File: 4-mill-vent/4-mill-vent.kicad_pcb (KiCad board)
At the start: 2 copper layers, 87 x 47.6 mm, 69 parts, among them J1 Fan, J2 Buszzer, J3 Power, J4 ICSP, Q1 MMBT3904, Q2 MMBT3904, Q3 PZT3904, Q4 PZT3904, Q5 TSM480P06CP, Q6 MMBT3904, SW1 Power_off, SW2 Power_On, SW3 Fan_Down, SW4 Fan_Up, U1 LM321, U2 TSR_1-24120, U3 LM1117-5.0, U4 ATmega328P-AU, Y1 16.000MHZ

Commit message: Save point
Lots done, still working on some of the design so parts of micro are still up in air. Looks like this board size will for and can be made smaller
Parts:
- added C15: C0603C104M4RACTU, Capacitor_SMD:C_0603_1608Metric, F.Cu at (290.1, 172.7)
- added C16: C0603C104M4RACTU, Capacitor_SMD:C_0603_1608Metric, F.Cu at (283.4, 172.7)
- added R22: 10k, Resistor_SMD:R_0603_1608Metric, F.Cu at (283.4, 174.6)
- added R23: 10k, Resistor_SMD:R_0603_1608Metric, F.Cu at (290.1, 174.6)
- J2: value Buszzer -> Buzzer
- moved R12 102.2 mm to (322.8, 158.2)
- moved Q4 97.7 mm to (322.4, 167.5)
- moved Motor1 96.3 mm to (323.6, 181.0)
- moved D2 96.2 mm to (322.3, 176.5)
- moved R11 96.0 mm to (322.5, 153.4)
- moved R1 81.3 mm to (322.1, 148.9)
- moved R20 80.0 mm to (290.9, 169.1)
- moved C13 78.8 mm to (299.8, 153.7), turned to 270 degrees
- moved R19 75.6 mm to (282.6, 169.1)
- moved R21 64.6 mm to (280.5, 153.9), turned to 90 degrees
- moved J4 62.2 mm to (272.7, 156.2), turned to 180 degrees
- moved C12 47.0 mm to (248.1, 167.9)
- moved C2 47.0 mm to (250.4, 177.8)
- moved C3 47.0 mm to (251.0, 180.5)
- moved C5 47.0 mm to (250.2, 168.6)
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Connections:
- J2 pad 1: SW_Batt -> Buzzer-
- J2 pad 2: Buzzer- -> SW_Batt
- J3 pad 1: Net-(D13-Pad1) -> Net-(D13-Pad2)
- J3 pad 3: Net-(D13-Pad2) -> Net-(D13-Pad1)
- R19 pad 1: Down -> Net-(C16-Pad1)
- R20 pad 1: Up -> Net-(C15-Pad1)
- SW3 pad 2: Down -> Net-(C16-Pad1)
- SW4 pad 2: Up -> Net-(C15-Pad1)
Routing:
- net Monitor: track 23.2 -> 54.2 mm, vias 0 -> 1
- net +5V: track 116.0 -> 141.2 mm, vias 5 -> 6
- net Net-(R12-Pad1): track 24.8 -> 0.00 mm
- net Net-(D2-Pad2): track 19.8 -> 0.00 mm
- net Down: track 12.4 -> 0.00 mm, vias 1 -> 0
- net Buzzer-: track 26.5 -> 16.7 mm
- net Net-(Q5-Pad1): track 6.53 -> 15.6 mm
- net Net-(D2-Pad1): track 8.34 -> 0.00 mm
- net Net-(C15-Pad1): track 0.00 -> 7.66 mm
- net Net-(C16-Pad1): track 0.00 -> 7.50 mm
- net Up: track 6.49 -> 0.00 mm, vias 1 -> 0
- net Net-(Q3-Pad1): track 1.65 -> 7.80 mm
- net Net-(Q4-Pad1): track 5.69 -> 0.00 mm
- net Reset: track 3.28 -> 8.03 mm
- net Raw_Batt: track 35.9 -> 31.9 mm, vias 3 -> 2
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
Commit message: Just pushing updates
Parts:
- moved D8 0.23 mm to (277.7, 153.6)
- moved D9 0.20 mm to (286.8, 153.7)
- moved R21 0.16 mm to (280.5, 153.7)
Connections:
- R23 pad 1: Net-(R23-Pad1) -> Up
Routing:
- net Up: track 0.00 -> 30.8 mm, vias 0 -> 1
- net Down: track 0.00 -> 28.9 mm, vias 0 -> 1
- net +5V: track 141.2 -> 167.4 mm
- net +12V: track 46.5 -> 53.6 mm
- net Net-(C15-Pad1): track 7.66 -> 14.0 mm
- net GND: vias 42 -> 43

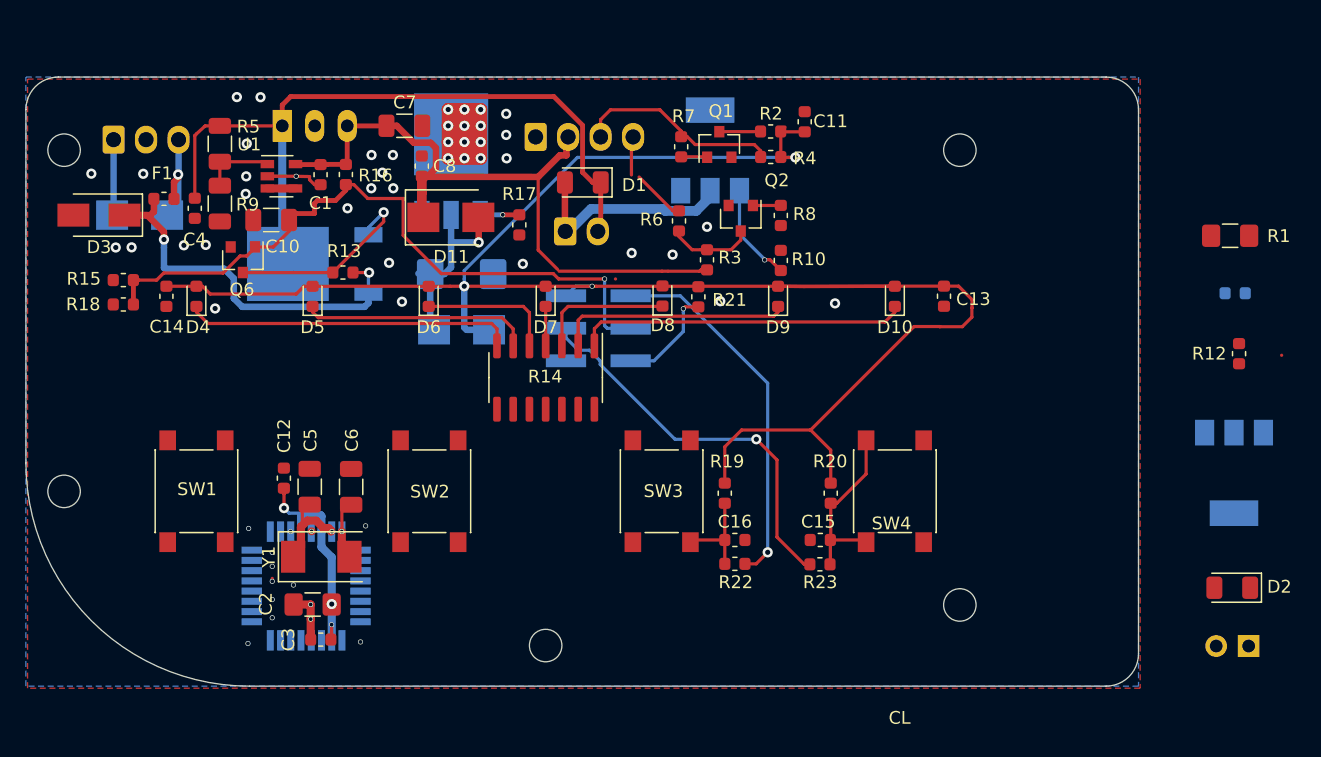
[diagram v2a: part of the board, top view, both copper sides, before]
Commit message: Just an update on things
update schematic to and pcb. figured out a way to user int, ext and chager over three pin connector with only to wires to PCB and no extra diode needed. getting closer to the anwers on PWM pins to use with what fuction.
very little let to do on PCB, but things have to get checked before getting it done.
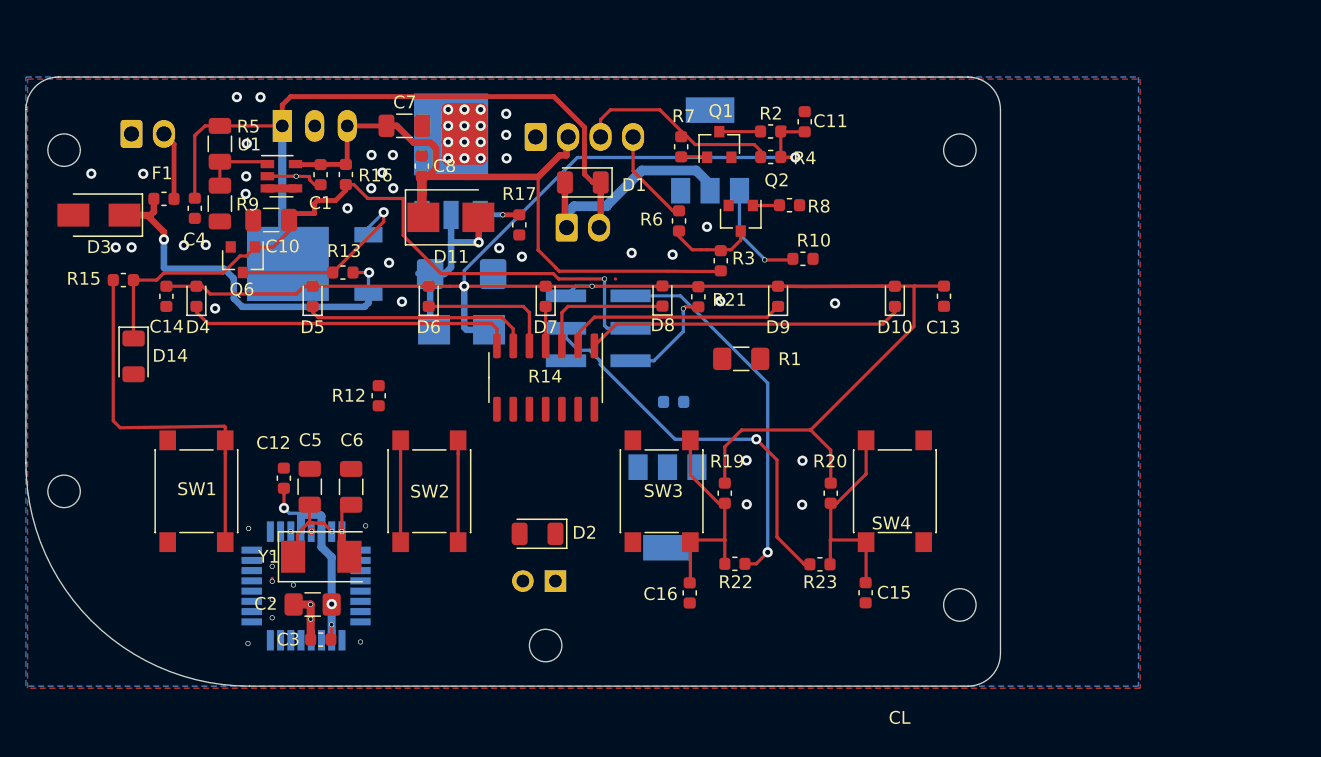
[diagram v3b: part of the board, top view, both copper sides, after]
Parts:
- removed D13: FM4004-W, Diode_SMD:D_SMB
- removed R18: 1k, Resistor_SMD:R_0603_1608Metric
- added D14: 1N914, Diode_SMD:D_1206_3216Metric, F.Cu at (236.4, 158.4)
- D3: value SML4752HE3_A/I -> 833-3SMAJ5936B-TP
- J3: value Power -> POWER_CONNECTOR; footprint Connector_Molex:Molex_KK-254_AE-6410-03A_1x03_P2.54mm_Vertical -> Connector_Molex:Molex_KK-254_AE-6410-02A_1x02_P2.54mm_Vertical
- U2: value TSR_1-24120 -> TPSM84212EAB
- moved R12 67.4 mm to (255.5, 161.4)
- moved D2 54.5 mm to (268.0, 172.2)
- moved Motor1 54.4 mm to (269.4, 175.9)
- moved R11 44.7 mm to (278.6, 161.9), turned to 180 degrees
- moved Q4 44.4 mm to (278.1, 170.2)
- moved R1 39.4 mm to (283.9, 158.6)
- moved C15 5.44 mm to (293.6, 176.8), turned to 270 degrees
- moved C16 5.44 mm to (279.9, 176.9), turned to 270 degrees
- moved R10 1.74 mm to (288.7, 150.7), turned to 0 degrees
- moved J3 1.47 mm to (236.2, 141.0)
- moved R3 1.08 mm to (282.3, 150.9)
- moved R8 1.05 mm to (287.7, 146.5), turned to 180 degrees
- moved J2 0.31 mm to (270.2, 148.3)
- turned U4 to 0 degrees
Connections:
- C10 pad 1: Monitor -> Monitor_SCLK
- F1 pad 1: Net-(D13-Pad1) -> Net-(F1-Pad1)
- J3 pad 1: Net-(D13-Pad2) -> GND
- J3 pad 2: GND -> Net-(F1-Pad1)
- J4 pad 1: Down -> Up_MOSI
- J4 pad 3: Monitor -> Monitor_SCLK
- J4 pad 4: Up -> Down+MOSO
- Q6 pad 1: Monitor -> Monitor_SCLK
- R15 pad 1: Monitor -> Monitor_SCLK
- R16 pad 1: Monitor -> Monitor_SCLK
- R22 pad 2: Down -> Down+MOSO
- R23 pad 1: Up -> Up_MOSI
- SW2 pad 1: Net-(R15-Pad2) -> Monitor_SCLK
- U4 pad 12: Monitor -> Net-(U4-Pad12)
- U4 pad 13: Motor -> Net-(U4-Pad13)
- U4 pad 15: Up -> Up_MOSI
- U4 pad 16: Down -> Down+MOSO
- U4 pad 17: Monitor -> Monitor_SCLK
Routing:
- net Net-(R15-Pad2): track 0.00 -> 29.0 mm
- net Net-(C16-Pad1): track 7.50 -> 17.0 mm
- net Net-(D13-Pad1): track 8.05 -> 0.00 mm, vias 2 -> 1
- net Net-(R12-Pad1): track 0.00 -> 7.96 mm
- net Monitor_SCLK: track 0.00 -> 7.96 mm
- net Net-(D13-Pad2): track 5.95 -> 0.00 mm
- net +5V: track 167.4 -> 161.8 mm
- net Net-(F1-Pad1): track 0.00 -> 5.41 mm
- net Net-(C5-Pad1): track 11.9 -> 7.88 mm
- net Net-(C15-Pad1): track 14.0 -> 17.2 mm
- net Monitor: track 54.2 -> 56.9 mm
- net Buzzer-: track 16.7 -> 18.5 mm
- net Net-(D9-Pad1): track 18.3 -> 17.5 mm
- net Net-(D10-Pad1): track 25.8 -> 25.0 mm
- net +12V: track 53.6 -> 54.3 mm
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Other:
- board size 87 x 47.6 mm -> 76.2 x 47.6 mm

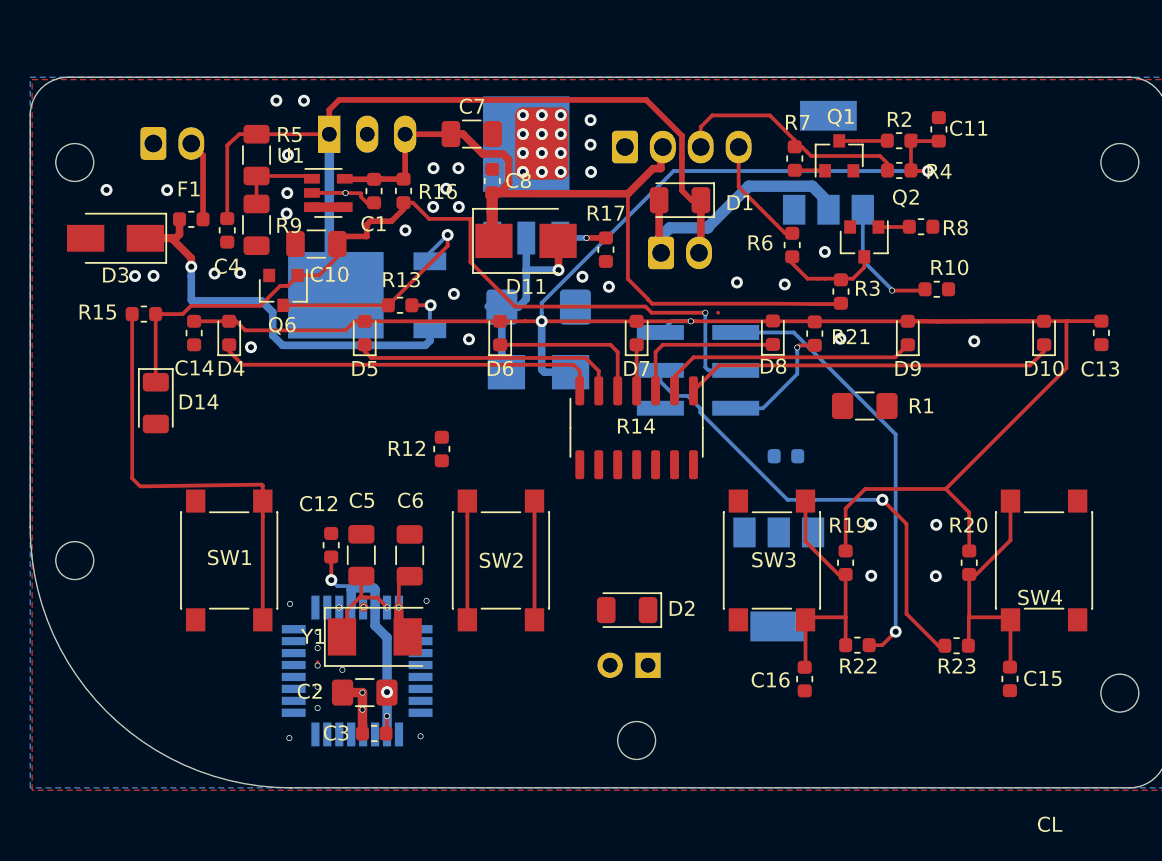
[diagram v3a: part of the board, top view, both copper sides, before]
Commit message: Board mainly done
Layout is done, have things to correct and adjustments to make, but for the most part it is done.
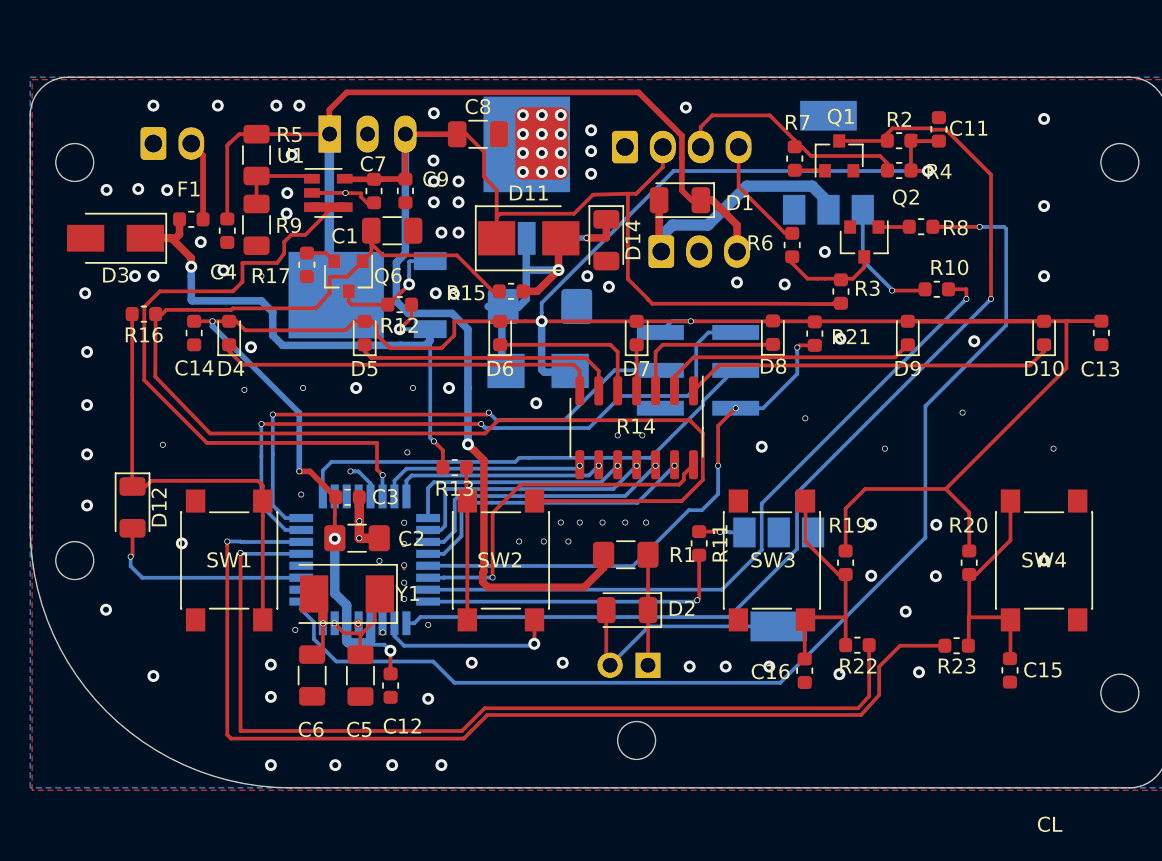
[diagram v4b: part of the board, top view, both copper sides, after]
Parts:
- added D13: FM4004-W, Diode_SMD:D_SMB, B.Cu at (262.0, 156.2)
- C10: value 1uF -> T491C107M006AT; footprint Capacitor_SMD:C_1206_3216Metric -> Capacitor_Tantalum_SMD:CP_EIA-6032-15_Kemet-U; moved to B.Cu
- C7: value LMK316AB7106MLHT -> 3.3uF
- C8: value C0603C104M4RACTU -> LMK316AB7106MLHT; footprint Capacitor_SMD:C_0603_1608Metric -> Capacitor_SMD:C_1206_3216Metric
- C9: value T491C107M006AT -> C0603C104M4RACTU; footprint Capacitor_Tantalum_SMD:CP_EIA-6032-15_Kemet-U -> Capacitor_SMD:C_0603_1608Metric; moved to F.Cu
- D12: value FM4004-W -> 1N914; footprint Diode_SMD:D_SMB -> Diode_SMD:D_1206_3216Metric; moved to F.Cu
- J2: footprint Connector_Molex:Molex_KK-254_AE-6410-02A_1x02_P2.54mm_Vertical -> Connector_Molex:Molex_KK-254_AE-6410-03A_1x03_P2.54mm_Vertical
- J3: value POWER_CONNECTOR -> Power
- R11: moved to F.Cu
- R12: value 100k -> 560k
- R15: value 1M -> 820k
- R16: value 10k -> 220k
- R17: value 47 -> 560k
- R5: value RN73H2BTTD4702B10 -> RN73H2BTTD4322F100
- R9: value RN73H2BTTD7061B10 -> RN73H2BTTD8061F50
- moved D14 32.1 mm to (266.6, 147.4)
- moved D12 28.7 mm to (234.8, 165.4), turned to 270 degrees
- moved R15 24.7 mm to (260.2, 150.9), turned to 0 degrees
- moved R17 20.1 mm to (246.5, 149.1), turned to 270 degrees
- moved R16 19.3 mm to (235.6, 152.4), turned to 180 degrees
- moved R1 18.9 mm to (267.9, 168.5)
- moved C3 15.9 mm to (249.2, 164.7), turned to 180 degrees
- moved C10 15.6 mm to (262.1, 151.9), turned to 0 degrees
- moved C9 11.8 mm to (253.1, 144.1), turned to 270 degrees
- moved R13 11.5 mm to (256.4, 162.7)
- moved C6 10.4 mm to (246.9, 176.6), turned to 270 degrees
- moved C2 10.4 mm to (249.9, 167.4), turned to 180 degrees
- moved C12 10.2 mm to (252.1, 177.3), turned to 270 degrees
- moved R12 10.1 mm to (252.7, 151.8), turned to 180 degrees
- moved C7 8.39 mm to (252.2, 146.8)
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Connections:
- net REF renamed Net-(U4-Pad20)
- C10 pad 1: Monitor_SCLK -> Net-(C10-Pad1)
- C7 pad 1: +12V -> Monitor
- C9 pad 1: Net-(C9-Pad1) -> +12V
- D11 pad 2: Net-(C9-Pad1) -> Net-(C10-Pad1)
- D12 pad 1: +5V -> Net-(D12-Pad1)
- D12 pad 2: Net-(C9-Pad1) -> Micro_power_Down
- D14 pad 1: Monitor -> Net-(D14-Pad1)
- D14 pad 2: Micro_power_Down -> GND
- J2 pad 2: SW_Batt -> Net-(J2-Pad2)
- J4 pad 1: Up_MOSI -> MOSI
- J4 pad 3: Monitor_SCLK -> SCLK
- J4 pad 4: Down+MOSO -> MOSO
- Q6 pad 1: Monitor_SCLK -> Monitor
- Q6 pad 2: GND -> Net-(Q6-Pad2)
- R12 pad 1: Net-(R12-Pad1) -> Raw_Batt
- R12 pad 2: Raw_Batt -> Net-(Q5-Pad1)
- R13 pad 1: Raw_Batt -> Net-(R13-Pad1)
- R13 pad 2: Net-(Q5-Pad1) -> Raw_Batt
- R14 pad 11: Error -> LED4
- R15 pad 1: Monitor_SCLK -> Monitor
- R15 pad 2: Net-(R15-Pad2) -> Net-(C10-Pad1)
- R16 pad 1: Monitor_SCLK -> Monitor
- R16 pad 2: +12V -> Net-(D12-Pad1)
- R17 pad 1: GND -> Net-(Q6-Pad2)
- R17 pad 2: Net-(R17-Pad2) -> GND
- R22 pad 2: Down+MOSO -> Down
- R23 pad 1: Up_MOSI -> Up
- SW1 pad 2: Net-(R15-Pad2) -> Net-(D12-Pad1)
- SW2 pad 1: Monitor_SCLK -> Monitor
- SW2 pad 2: Net-(R12-Pad1) -> Net-(R13-Pad1)
- U3 pad 1: Net-(R17-Pad2) -> Net-(D14-Pad1)
- U3 pad 2: Net-(C9-Pad1) -> Net-(C10-Pad1)
- U4 pad 1: Net-(U4-Pad1) -> RPM
- U4 pad 11: Net-(U4-Pad11) -> Micro_power_Down
- U4 pad 13: Net-(U4-Pad13) -> Down
- U4 pad 14: Net-(U4-Pad14) -> Up
- U4 pad 15: Up_MOSI -> MOSI
- U4 pad 16: Down+MOSO -> MOSO
- U4 pad 17: Monitor_SCLK -> SCLK
- U4 pad 2: Net-(U4-Pad2) -> Monitor
- U4 pad 23: Net-(U4-Pad23) -> LED1
- U4 pad 24: Net-(U4-Pad24) -> LED2
- U4 pad 25: Net-(U4-Pad25) -> LED3
- U4 pad 26: Net-(U4-Pad26) -> LED4
- U4 pad 27: Net-(U4-Pad27) -> LED5
- U4 pad 28: Net-(U4-Pad28) -> LED6
- U4 pad 30: Net-(U4-Pad30) -> LED7
- U4 pad 31: Net-(U4-Pad31) -> Alarm
- U4 pad 32: Net-(U4-Pad32) -> Motor
- U4 pad 9: Net-(U4-Pad9) -> PWM
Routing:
- net PWM: track 0.00 -> 77.0 mm, vias 0 -> 1
- net RPM: track 3.26 -> 70.8 mm, vias 0 -> 1
- net Net-(C10-Pad1): track 0.00 -> 50.5 mm, vias 0 -> 13
- net Alarm: track 0.00 -> 47.8 mm, vias 0 -> 1
- net Net-(C9-Pad1): track 47.5 -> 0.00 mm, vias 13 -> 0
- net MOSI: track 0.00 -> 45.1 mm, vias 0 -> 2
- net +12V: track 54.3 -> 98.3 mm, vias 0 -> 1
- net Batt_V: track 2.20 -> 45.7 mm, vias 0 -> 1
- net Monitor: track 56.9 -> 99.4 mm
- net Up: track 30.8 -> 69.8 mm
- net MOSO: track 0.00 -> 36.0 mm, vias 0 -> 2
- net Down: track 28.9 -> 62.6 mm
- net SCLK: track 0.00 -> 32.3 mm
- net Net-(D12-Pad1): track 0.00 -> 29.8 mm
- net Net-(R15-Pad2): track 29.0 -> 0.00 mm
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
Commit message: lastest updates to board
Board is done, just need to do more checking
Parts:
- moved C1 145.7 mm to (122.2, 76.0)
- moved C11 145.7 mm to (160.1, 71.8)
- moved C15 145.7 mm to (164.8, 108.1)
- moved C4 145.7 mm to (112.4, 78.6)
- moved C6 145.7 mm to (118.1, 108.4)
- moved D12 145.7 mm to (106.0, 97.2)
- moved D2 145.7 mm to (139.2, 104.0)
- moved R13 145.7 mm to (127.6, 94.5)
- moved R14 145.7 mm to (139.8, 91.8)
- moved R16 145.7 mm to (106.8, 84.2)
- moved R17 145.7 mm to (117.7, 80.9)
- moved R7 145.7 mm to (150.4, 73.8)
- moved R9 145.7 mm to (114.4, 78.2)
- moved U2 145.7 mm to (119.3, 72.1)
- moved C10 145.7 mm to (133.3, 83.7)
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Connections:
- J4 pad 1: MOSI -> MOSO
- J4 pad 4: MOSO -> MOSI
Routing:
- net MOSO: track 36.0 -> 43.2 mm
- net MOSI: track 45.1 -> 37.8 mm, vias 2 -> 4
- net PWM: track 77.0 -> 77.6 mm
- net +5V: vias 7 -> 8
- net GND: vias 106 -> 128
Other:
- board text added: "K9DTV"
- board text added: "Pin 1"
- board text removed: "CL"
